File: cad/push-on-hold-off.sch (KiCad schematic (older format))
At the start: 12 parts

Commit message: Annotate schematic
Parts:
- gave numbers to parts that had none: 11
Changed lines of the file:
@@
 LIBS:contrib
 LIBS:valves
+LIBS:push-on-hold-off-cache
 EELAYER 25 0
 EELAYER END
@@
 $EndDescr
 $Comp
-L IRF7309IPBF Q?
+L IRF7309IPBF Q1
 U 1 1 569FBD83
 P 6050 4300
-F 0 "Q?" H 6300 4375 50  0000 L CNN
+F 0 "Q1" H 6300 4375 50  0000 L CNN
 F 1 "IRF7309IPBF" H 6300 4300 50  0000 L CNN
 F 2 "SO-8" H 6300 4225 50  0000 L CNN
@@
 $EndComp
 $Comp
-L IRF7309IPBF Q?
+L IRF7309IPBF Q1
 U 2 1 569FBDAC
 P 6000 3700
-F 0 "Q?" H 6250 3775 50  0000 L CNN
+F 0 "Q1" H 6250 3775 50  0000 L CNN
 F 1 "IRF7309IPBF" H 6250 3700 50  0000 L CNN
 F 2 "SO-8" H 6250 3625 50  0000 L CNN
@@
 $EndComp
 $Comp
-L CONN_01X04 P?
+L CONN_01X04 P1
 U 1 1 569FC392
 P 4450 3750
-F 0 "P?" H 4450 4000 50  0000 C CNN
+F 0 "P1" H 4450 4000 50  0000 C CNN
 F 1 "CONN_01X04" V 4550 3750 50  0000 C CNN
 F 2 "" H 4450 3750 60  0000 C CNN
@@
 $EndComp
 $Comp
-L R R?
+L R R1
 U 1 1 569FC430
 P 5050 3800
-F 0 "R?" V 5130 3800 50  0000 C CNN
+F 0 "R1" V 5130 3800 50  0000 C CNN
 F 1 "10k" V 5050 3800 50  0000 C CNN
 F 2 "" V 4980 3800 30  0000 C CNN
@@
 $EndComp
 $Comp
-L R R?
+L R R2
 U 1 1 569FC492
 P 5650 3800
-F 0 "R?" V 5730 3800 50  0000 C CNN
+F 0 "R2" V 5730 3800 50  0000 C CNN
 F 1 "100k" V 5650 3800 50  0000 C CNN
 F 2 "" V 5580 3800 30  0000 C CNN
@@
 	4650 3600 5800 3600
 $Comp
-L C C?
+L C C1
 U 1 1 569FC537
 P 5350 4100
-F 0 "C?" H 5375 4200 50  0000 L CNN
+F 0 "C1" H 5375 4200 50  0000 L CNN
 F 1 "1uF" H 5375 4000 50  0000 L CNN
 F 2 "" H 5388 3950 30  0000 C CNN
@@
 	5950 4100 5950 3900
 $Comp
-L GND #PWR?
+L GND #PWR1
 U 1 1 569FC7CE
 P 4700 4050
-F 0 "#PWR?" H 4700 3800 50  0001 C CNN
+F 0 "#PWR1" H 4700 3800 50  0001 C CNN
 F 1 "GND" H 4700 3900 50  0000 C CNN
 F 2 "" H 4700 4050 60  0000 C CNN
@@
 Wire Wire Line
 	4850 4100 5200 4100
-Text Label 4750 3700 0    60   ~ 0
+Text Label 4650 3700 0    60   ~ 0
 Button
 $Comp
-L D D?
+L D D1
 U 1 1 569FCB4E
 P 4850 4400
-F 0 "D?" H 4850 4500 50  0000 C CNN
+F 0 "D1" H 4850 4500 50  0000 C CNN
 F 1 "D" H 4850 4300 50  0000 C CNN
 F 2 "" H 4850 4400 60  0000 C CNN
@@
 Connection ~ 5850 4100
 $Comp
-L GND #PWR?
+L GND #PWR2
 U 1 1 569FCD58
 P 5950 4550
-F 0 "#PWR?" H 5950 4300 50  0001 C CNN
+F 0 "#PWR2" H 5950 4300 50  0001 C CNN
 F 1 "GND" H 5950 4400 50  0000 C CNN
 F 2 "" H 5950 4550 60  0000 C CNN
@@
 	5950 4500 5950 4550
 $Comp
-L C C?
+L C C2
 U 1 1 569FCE3F
 P 6500 3950
-F 0 "C?" H 6525 4050 50  0000 L CNN
+F 0 "C2" H 6525 4050 50  0000 L CNN
 F 1 "10uF" H 6525 3850 50  0000 L CNN
 F 2 "" H 6538 3800 30  0000 C CNN
@@
 Connection ~ 6300 3600
 $Comp
-L CONN_01X04 P?
+L CONN_01X04 P2
 U 1 1 569FCF63
 P 7750 3750
-F 0 "P?" H 7750 4000 50  0000 C CNN
+F 0 "P2" H 7750 4000 50  0000 C CNN
 F 1 "CONN_01X04" V 7850 3750 50  0000 C CNN
 F 2 "" H 7750 3750 60  0000 C CNN
@@
 $EndComp
 $Comp
-L R R?
+L R R4
 U 1 1 569FD783
 P 6950 3950
-F 0 "R?" V 7030 3950 50  0000 C CNN
+F 0 "R4" V 7030 3950 50  0000 C CNN
 F 1 "100k" V 6950 3950 50  0000 C CNN
 F 2 "" V 6880 3950 30  0000 C CNN
@@
 Connection ~ 6500 4350
 $Comp
-L R R?
+L R R3
 U 1 1 569FD864
 P 6700 4350
-F 0 "R?" V 6780 4350 50  0000 C CNN
+F 0 "R3" V 6780 4350 50  0000 C CNN
 F 1 "300k" V 6700 4350 50  0000 C CNN
 F 2 "" V 6630 4350 30  0000 C CNN
@@
 Text Label 7300 3600 0    60   ~ 0
 Vout
-Text Label 4750 3600 0    60   ~ 0
+Text Label 4650 3600 0    60   ~ 0
 Vin
 Text Label 7300 3700 0    60   ~ 0
@@
 	7550 3700 7300 3700
 $Comp
-L GND #PWR?
+L GND #PWR4
 U 1 1 569FDE5F
 P 7450 3950
-F 0 "#PWR?" H 7450 3700 50  0001 C CNN
+F 0 "#PWR4" H 7450 3700 50  0001 C CNN
 F 1 "GND" H 7450 3800 50  0000 C CNN
 F 2 "" H 7450 3950 60  0000 C CNN
@@
 Connection ~ 6950 4350
 $Comp
-L SW_PUSH_SMALL SW?
+L SW_PUSH_SMALL SW1
 U 1 1 569FEA9F
 P 5950 5350
-F 0 "SW?" H 6100 5460 30  0000 C CNN
+F 0 "SW1" H 6100 5460 30  0000 C CNN
 F 1 "SW_PUSH_SMALL" H 5950 5271 30  0000 C CNN
 F 2 "" H 5950 5350 60  0000 C CNN
@@
 $EndComp
 $Comp
-L GND #PWR?
+L GND #PWR3
 U 1 1 569FECE2
 P 6100 5500
-F 0 "#PWR?" H 6100 5250 50  0001 C CNN
+F 0 "#PWR3" H 6100 5250 50  0001 C CNN
 F 1 "GND" H 6100 5350 50  0000 C CNN
 F 2 "" H 6100 5500 60  0000 C CNN

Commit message: Start layout
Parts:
- C1, C2: footprint (none) -> Capacitors_SMD.pretty:C_0603_HandSoldering
- D1: footprint (none) -> Diodes_SMD.pretty:SOD-323; Farnell (none) -> 1466524
- P1, P2: footprint (none) -> Pin_Headers.pretty:Pin_Header_Straight_1x04
- Q1: footprint SO-8 -> Housings_SOIC.pretty:SOIJ-8_5.3x5.3mm_Pitch1.27mm; Farnell (none) -> 2468006
- Q1: footprint SO-8 -> Housings_SOIC.pretty:SOIJ-8_5.3x5.3mm_Pitch1.27mm
- R1, R2, R3, R4: footprint (none) -> Resistors_SMD.pretty:R_0603_HandSoldering
- SW1: footprint (none) -> Buttons_Switches_SMD.pretty:SW_SPST_EVPBF; Farnell (none) -> 3801305
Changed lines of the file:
@@
 F 0 "Q1" H 6300 4375 50  0000 L CNN
 F 1 "IRF7309IPBF" H 6300 4300 50  0000 L CNN
-F 2 "SO-8" H 6300 4225 50  0000 L CNN
+F 2 "Housings_SOIC.pretty:SOIJ-8_5.3x5.3mm_Pitch1.27mm" H 6300 4225 50  0000 L CNN
 F 3 "" H 6050 4300 50  0000 L CNN
+F 4 "2468006" H 6050 4300 60  0001 C CNN "Farnell"
 	1    6050 4300
 	-1   0    0    -1
@@
 F 0 "Q1" H 6250 3775 50  0000 L CNN
 F 1 "IRF7309IPBF" H 6250 3700 50  0000 L CNN
-F 2 "SO-8" H 6250 3625 50  0000 L CNN
+F 2 "Housings_SOIC.pretty:SOIJ-8_5.3x5.3mm_Pitch1.27mm" H 6250 3625 50  0000 L CNN
 F 3 "" H 6000 3700 50  0000 L CNN
 	2    6000 3700
@@
 F 0 "P1" H 4450 4000 50  0000 C CNN
 F 1 "CONN_01X04" V 4550 3750 50  0000 C CNN
-F 2 "" H 4450 3750 60  0000 C CNN
+F 2 "Pin_Headers.pretty:Pin_Header_Straight_1x04" H 4450 3750 60  0001 C CNN
 F 3 "" H 4450 3750 60  0000 C CNN
 	1    4450 3750
@@
 F 0 "R1" V 5130 3800 50  0000 C CNN
 F 1 "10k" V 5050 3800 50  0000 C CNN
-F 2 "" V 4980 3800 30  0000 C CNN
+F 2 "Resistors_SMD.pretty:R_0603_HandSoldering" V 4980 3800 30  0001 C CNN
 F 3 "" H 5050 3800 30  0000 C CNN
 	1    5050 3800
@@
 F 0 "R2" V 5730 3800 50  0000 C CNN
 F 1 "100k" V 5650 3800 50  0000 C CNN
-F 2 "" V 5580 3800 30  0000 C CNN
+F 2 "Resistors_SMD.pretty:R_0603_HandSoldering" V 5580 3800 30  0001 C CNN
 F 3 "" H 5650 3800 30  0000 C CNN
 	1    5650 3800
@@
 F 0 "C1" H 5375 4200 50  0000 L CNN
 F 1 "1uF" H 5375 4000 50  0000 L CNN
-F 2 "" H 5388 3950 30  0000 C CNN
+F 2 "Capacitors_SMD.pretty:C_0603_HandSoldering" H 5388 3950 30  0001 C CNN
 F 3 "" H 5350 4100 60  0000 C CNN
 	1    5350 4100
@@
 	5950 4100 5950 3900
 $Comp
-L GND #PWR1
+L GND #PWR01
 U 1 1 569FC7CE
 P 4700 4050
-F 0 "#PWR1" H 4700 3800 50  0001 C CNN
+F 0 "#PWR01" H 4700 3800 50  0001 C CNN
 F 1 "GND" H 4700 3900 50  0000 C CNN
 F 2 "" H 4700 4050 60  0000 C CNN
@@
 F 0 "D1" H 4850 4500 50  0000 C CNN
 F 1 "D" H 4850 4300 50  0000 C CNN
-F 2 "" H 4850 4400 60  0000 C CNN
+F 2 "Diodes_SMD.pretty:SOD-323" H 4850 4400 60  0001 C CNN
 F 3 "" H 4850 4400 60  0000 C CNN
+F 4 "1466524" H 4850 4400 60  0001 C CNN "Farnell"
 	1    4850 4400
 	0    1    1    0
@@
 Connection ~ 5850 4100
 $Comp
-L GND #PWR2
+L GND #PWR02
 U 1 1 569FCD58
 P 5950 4550
-F 0 "#PWR2" H 5950 4300 50  0001 C CNN
+F 0 "#PWR02" H 5950 4300 50  0001 C CNN
 F 1 "GND" H 5950 4400 50  0000 C CNN
 F 2 "" H 5950 4550 60  0000 C CNN
@@
 F 0 "C2" H 6525 4050 50  0000 L CNN
 F 1 "10uF" H 6525 3850 50  0000 L CNN
-F 2 "" H 6538 3800 30  0000 C CNN
+F 2 "Capacitors_SMD.pretty:C_0603_HandSoldering" H 6538 3800 30  0001 C CNN
 F 3 "" H 6500 3950 60  0000 C CNN
 	1    6500 3950
@@
 F 0 "P2" H 7750 4000 50  0000 C CNN
 F 1 "CONN_01X04" V 7850 3750 50  0000 C CNN
-F 2 "" H 7750 3750 60  0000 C CNN
+F 2 "Pin_Headers.pretty:Pin_Header_Straight_1x04" H 7750 3750 60  0001 C CNN
 F 3 "" H 7750 3750 60  0000 C CNN
 	1    7750 3750
@@
 F 0 "R4" V 7030 3950 50  0000 C CNN
 F 1 "100k" V 6950 3950 50  0000 C CNN
-F 2 "" V 6880 3950 30  0000 C CNN
+F 2 "Resistors_SMD.pretty:R_0603_HandSoldering" V 6880 3950 30  0001 C CNN
 F 3 "" H 6950 3950 30  0000 C CNN
 	1    6950 3950
@@
 F 0 "R3" V 6780 4350 50  0000 C CNN
 F 1 "300k" V 6700 4350 50  0000 C CNN
-F 2 "" V 6630 4350 30  0000 C CNN
+F 2 "Resistors_SMD.pretty:R_0603_HandSoldering" V 6630 4350 30  0001 C CNN
 F 3 "" H 6700 4350 30  0000 C CNN
 	1    6700 4350
@@
 	7550 3700 7300 3700
 $Comp
-L GND #PWR4
+L GND #PWR03
 U 1 1 569FDE5F
 P 7450 3950
-F 0 "#PWR4" H 7450 3700 50  0001 C CNN
+F 0 "#PWR03" H 7450 3700 50  0001 C CNN
 F 1 "GND" H 7450 3800 50  0000 C CNN
 F 2 "" H 7450 3950 60  0000 C CNN
@@
 F 0 "SW1" H 6100 5460 30  0000 C CNN
 F 1 "SW_PUSH_SMALL" H 5950 5271 30  0000 C CNN
-F 2 "" H 5950 5350 60  0000 C CNN
+F 2 "Buttons_Switches_SMD.pretty:SW_SPST_EVPBF" H 5950 5350 60  0001 C CNN
 F 3 "" H 5950 5350 60  0000 C CNN
+F 4 "3801305" H 5950 5350 60  0001 C CNN "Farnell"
 	1    5950 5350
 	1    0    0    -1
 $EndComp
 $Comp
-L GND #PWR3
+L GND #PWR04
 U 1 1 569FECE2
 P 6100 5500
-F 0 "#PWR3" H 6100 5250 50  0001 C CNN
+F 0 "#PWR04" H 6100 5250 50  0001 C CNN
 F 1 "GND" H 6100 5350 50  0000 C CNN
 F 2 "" H 6100 5500 60  0000 C CNN

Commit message: Add silkscreen connection reference
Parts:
- D1: Farnell 1466524 -> (none); Vendor (none) -> 1466524
- Q1: Farnell 2468006 -> (none); Vendor (none) -> 2468006
- SW1: Farnell 3801305 -> (none); Vendor (none) -> 3801305
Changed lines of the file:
@@
 F 2 "Housings_SOIC.pretty:SOIJ-8_5.3x5.3mm_Pitch1.27mm" H 6300 4225 50  0000 L CNN
 F 3 "" H 6050 4300 50  0000 L CNN
-F 4 "2468006" H 6050 4300 60  0001 C CNN "Farnell"
+F 4 "2468006" H 6050 4300 60  0001 C CNN "Vendor"
 	1    6050 4300
 	-1   0    0    -1
@@
 F 2 "Diodes_SMD.pretty:SOD-323" H 4850 4400 60  0001 C CNN
 F 3 "" H 4850 4400 60  0000 C CNN
-F 4 "1466524" H 4850 4400 60  0001 C CNN "Farnell"
+F 4 "1466524" H 4850 4400 60  0001 C CNN "Vendor"
 	1    4850 4400
 	0    1    1    0
@@
 F 2 "Buttons_Switches_SMD.pretty:SW_SPST_EVPBF" H 5950 5350 60  0001 C CNN
 F 3 "" H 5950 5350 60  0000 C CNN
-F 4 "3801305" H 5950 5350 60  0001 C CNN "Farnell"
+F 4 "3801305" H 5950 5350 60  0001 C CNN "Vendor"
 	1    5950 5350
 	1    0    0    -1

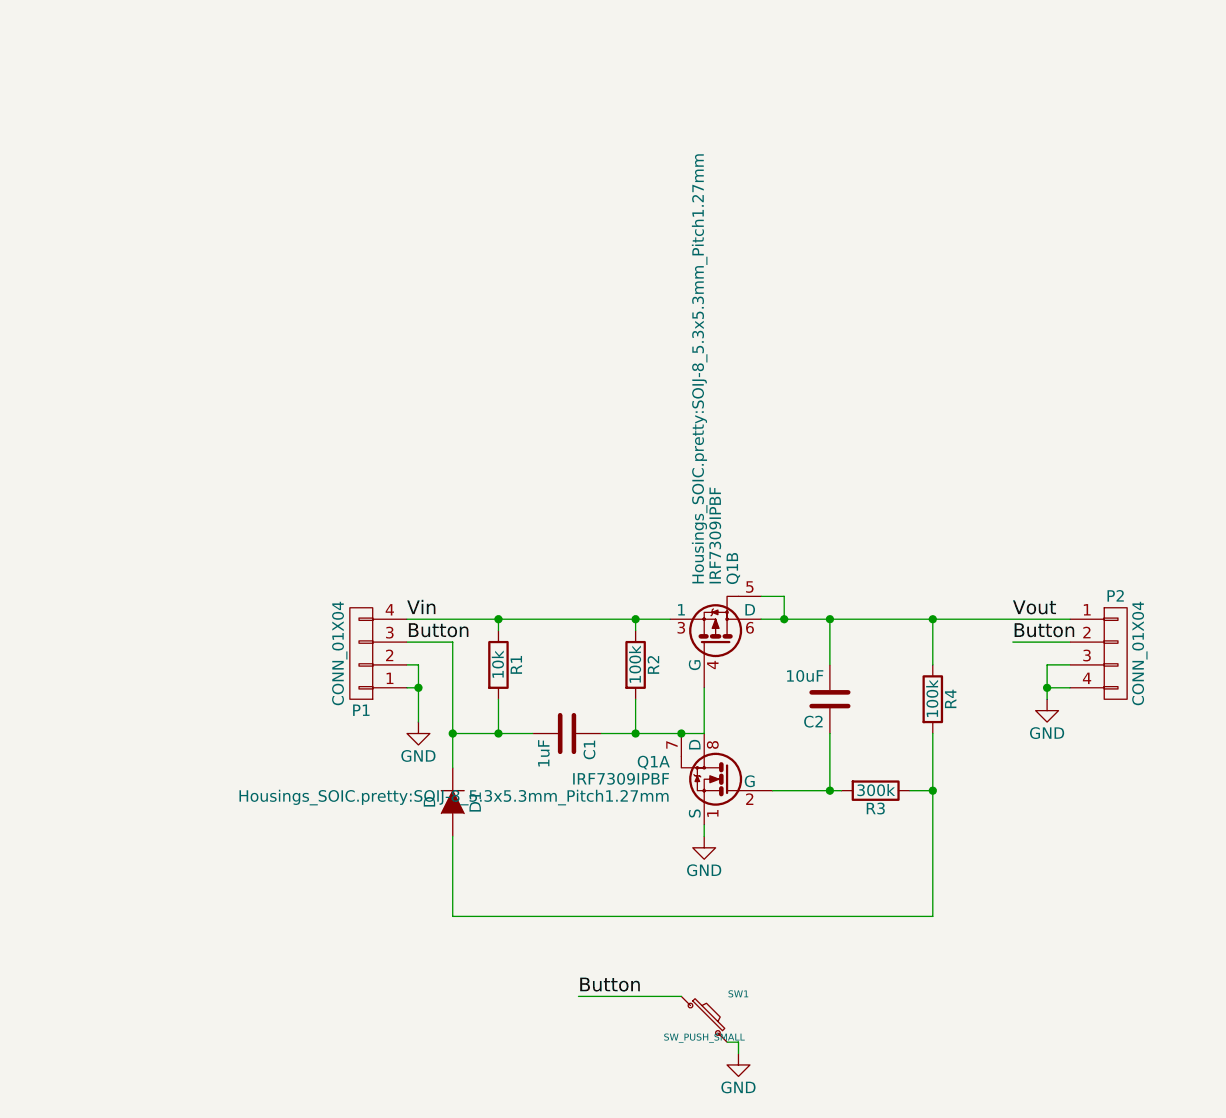
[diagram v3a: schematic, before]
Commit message: Add auto/on off caps and change Q1 footprint
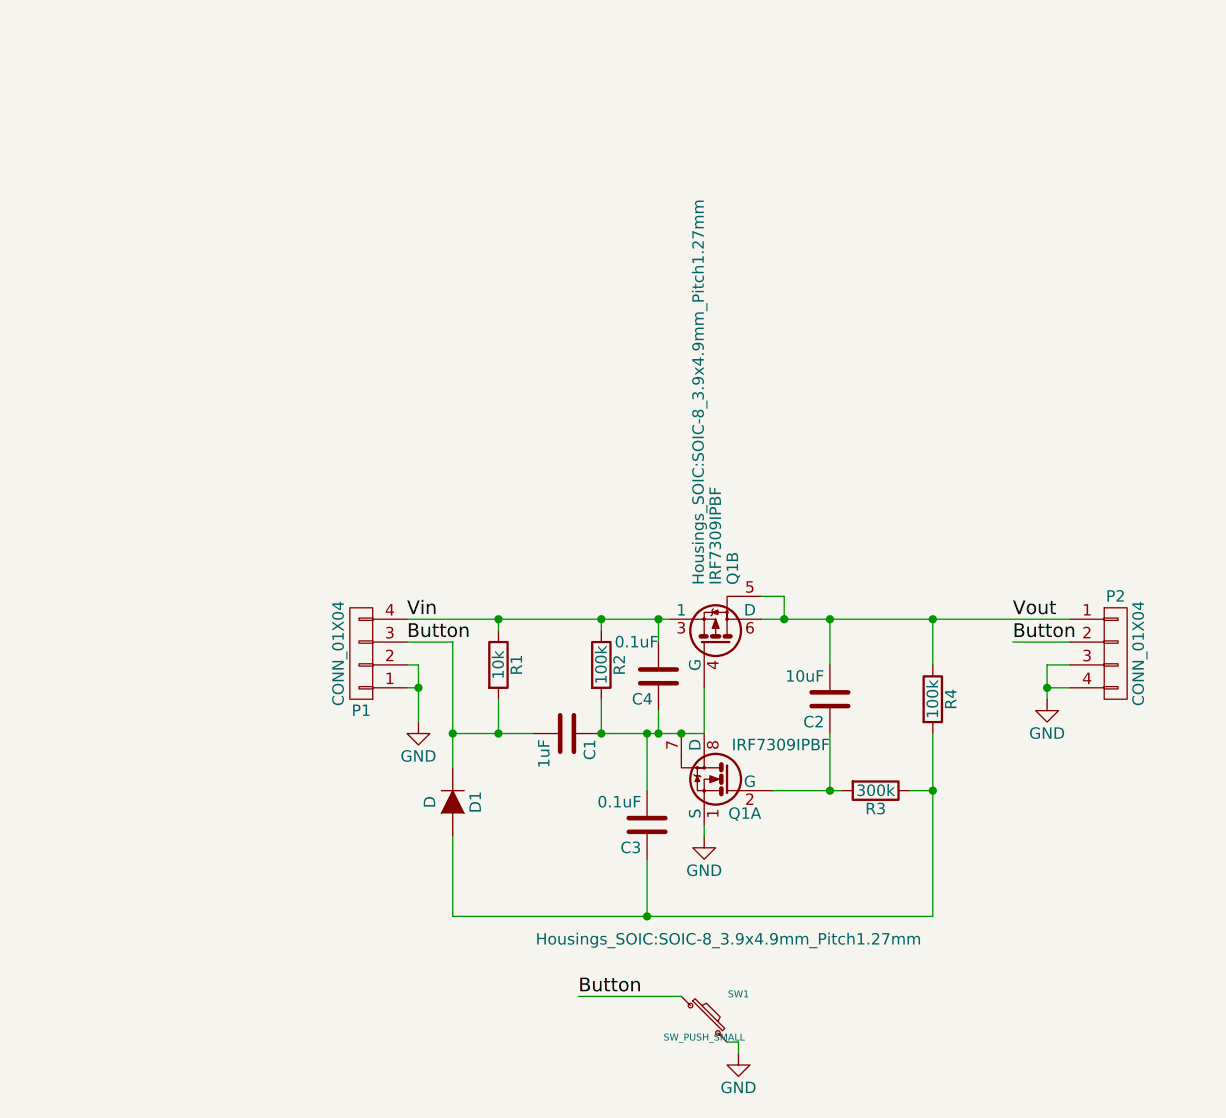
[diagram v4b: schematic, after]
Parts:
- added C3, C4: 0.1uF, Capacitors_SMD.pretty:C_0603_HandSoldering, symbol C
- Q1: footprint Housings_SOIC.pretty:SOIJ-8_5.3x5.3mm_Pitch1.27mm -> Housings_SOIC:SOIC-8_3.9x4.9mm_Pitch1.27mm
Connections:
- net Vin: now also C4.2
- net at C1.1, Q1.4 (G), Q1.7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: now also C3.2, C4.1
- net at D1.2 (A), R3.1, R4.2: now also C3.1
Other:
- moved on the sheet: R2
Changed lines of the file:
@@
 U 1 1 569FBD83
 P 6050 4300
-F 0 "Q1" H 6300 4375 50  0000 L CNN
-F 1 "IRF7309IPBF" H 6300 4300 50  0000 L CNN
-F 2 "Housings_SOIC.pretty:SOIJ-8_5.3x5.3mm_Pitch1.27mm" H 6300 4225 50  0000 L CNN
+F 0 "Q1" H 5900 4150 50  0000 L CNN
+F 1 "IRF7309IPBF" H 5600 4450 50  0000 L CNN
+F 2 "Housings_SOIC:SOIC-8_3.9x4.9mm_Pitch1.27mm" H 5200 3600 50  0000 L CNN
 F 3 "" H 6050 4300 50  0000 L CNN
 F 4 "2468006" H 6050 4300 60  0001 C CNN "Vendor"
@@
 F 0 "Q1" H 6250 3775 50  0000 L CNN
 F 1 "IRF7309IPBF" H 6250 3700 50  0000 L CNN
-F 2 "Housings_SOIC.pretty:SOIJ-8_5.3x5.3mm_Pitch1.27mm" H 6250 3625 50  0000 L CNN
+F 2 "Housings_SOIC:SOIC-8_3.9x4.9mm_Pitch1.27mm" H 6250 3625 50  0000 L CNN
 F 3 "" H 6000 3700 50  0000 L CNN
 	2    6000 3700
@@
 L R R2
 U 1 1 569FC492
-P 5650 3800
-F 0 "R2" V 5730 3800 50  0000 C CNN
-F 1 "100k" V 5650 3800 50  0000 C CNN
-F 2 "Resistors_SMD.pretty:R_0603_HandSoldering" V 5580 3800 30  0001 C CNN
-F 3 "" H 5650 3800 30  0000 C CNN
-	1    5650 3800
-	1    0    0    -1
-$EndComp
-Wire Wire Line
-	4650 3600 5800 3600
+P 5500 3800
+F 0 "R2" V 5580 3800 50  0000 C CNN
+F 1 "100k" V 5500 3800 50  0000 C CNN
+F 2 "Resistors_SMD.pretty:R_0603_HandSoldering" V 5430 3800 30  0001 C CNN
+F 3 "" H 5500 3800 30  0000 C CNN
+	1    5500 3800
+	1    0    0    -1
+$EndComp
 $Comp
 L C C1
@@
 	0    1    1    0
 $EndComp
-Wire Wire Line
-	5050 3650 5050 3600
-Connection ~ 5050 3600
-Connection ~ 5650 3600
-Wire Wire Line
-	5500 4100 5950 4100
-Wire Wire Line
-	5950 4100 5950 3900
 $Comp
 L GND #PWR01
@@
 	1    0    0    -1
 $EndComp
-Wire Wire Line
-	4650 3800 4700 3800
-Wire Wire Line
-	4700 3800 4700 4050
-Wire Wire Line
-	4650 3900 4700 3900
-Connection ~ 4700 3900
-Wire Wire Line
-	4650 3700 4850 3700
-Wire Wire Line
-	4850 3700 4850 4250
-Wire Wire Line
-	5650 3600 5650 3650
-Wire Wire Line
-	5650 3950 5650 4100
-Connection ~ 5650 4100
-Wire Wire Line
-	5050 3950 5050 4100
-Connection ~ 5050 4100
-Wire Wire Line
-	4850 4100 5200 4100
 Text Label 4650 3700 0    60   ~ 0
 Button
@@
 	0    1    1    0
 $EndComp
-Connection ~ 4850 4100
-Connection ~ 5850 4100
 $Comp
 L GND #PWR02
@@
 	1    0    0    -1
 $EndComp
-Wire Wire Line
-	5950 4500 5950 4550
 $Comp
 L C C2
@@
 	-1   0    0    1
 $EndComp
-Wire Wire Line
-	6500 4350 6500 4100
-Wire Wire Line
-	6500 3600 6500 3800
-Wire Wire Line
-	6200 3600 7550 3600
-Wire Wire Line
-	6300 3600 6300 3500
-Wire Wire Line
-	6300 3500 6200 3500
-Connection ~ 6300 3600
 $Comp
 L CONN_01X04 P2
@@
 	1    0    0    -1
 $EndComp
-Wire Wire Line
-	6950 3600 6950 3800
-Connection ~ 6500 3600
-Wire Wire Line
-	6950 4100 6950 4900
-Connection ~ 6500 4350
 $Comp
 L R R3
@@
 	0    1    1    0
 $EndComp
-Wire Wire Line
-	6250 4350 6550 4350
-Wire Wire Line
-	6950 4350 6850 4350
-Connection ~ 6950 3600
 Text Label 7300 3600 0    60   ~ 0
 Vout
@@
 Text Label 7300 3700 0    60   ~ 0
 Button
-Wire Wire Line
-	7550 3700 7300 3700
 $Comp
 L GND #PWR03
@@
 	1    0    0    -1
 $EndComp
-Wire Wire Line
-	7550 3900 7450 3900
-Wire Wire Line
-	7450 3800 7450 3950
-Wire Wire Line
-	7550 3800 7450 3800
-Connection ~ 7450 3900
-Wire Wire Line
-	4850 4550 4850 4900
-Wire Wire Line
-	4850 4900 6950 4900
-Connection ~ 6950 4350
 $Comp
 L SW_PUSH_SMALL SW1
@@
 	1    0    0    -1
 $EndComp
-Wire Wire Line
-	6050 5450 6100 5450
-Wire Wire Line
-	6100 5450 6100 5500
 Text Label 5400 5250 0    60   ~ 0
 Button
+$Comp
+L C C4
+U 1 1 57563AC8
+P 5750 3850
+F 0 "C4" H 5775 3950 50  0000 L CNN
+F 1 "0.1uF" H 5750 3700 50  0000 L CNN
+F 2 "Capacitors_SMD.pretty:C_0603_HandSoldering" H 5788 3700 30  0001 C CNN
+F 3 "" H 5750 3850 60  0000 C CNN
+	1    5750 3850
+	-1   0    0    1
+$EndComp
+$Comp
+L C C3
+U 1 1 57563BCA
+P 5700 4500
+F 0 "C3" H 5725 4600 50  0000 L CNN
+F 1 "0.1uF" H 5725 4400 50  0000 L CNN
+F 2 "Capacitors_SMD.pretty:C_0603_HandSoldering" H 5738 4350 30  0001 C CNN
+F 3 "" H 5700 4500 60  0000 C CNN
+	1    5700 4500
+	-1   0    0    1
+$EndComp
+Wire Wire Line
+	4650 3600 5800 3600
+Wire Wire Line
+	5050 3650 5050 3600
+Connection ~ 5050 3600
+Connection ~ 5500 3600
+Wire Wire Line
+	5500 4100 5950 4100
+Wire Wire Line
+	5950 4100 5950 3900
+Wire Wire Line
+	4650 3800 4700 3800
+Wire Wire Line
+	4700 3800 4700 4050
+Wire Wire Line
+	4650 3900 4700 3900
+Connection ~ 4700 3900
+Wire Wire Line
+	4650 3700 4850 3700
+Wire Wire Line
+	4850 3700 4850 4250
+Wire Wire Line
+	5500 3600 5500 3650
+Wire Wire Line
+	5500 3950 5500 4100
+Connection ~ 5500 4100
+Wire Wire Line
+	5050 3950 5050 4100
+Connection ~ 5050 4100
+Wire Wire Line
+	4850 4100 5200 4100
+Connection ~ 4850 4100
+Connection ~ 5850 4100
+Wire Wire Line
+	5950 4500 5950 4550
+Wire Wire Line
+	6500 4350 6500 4100
+Wire Wire Line
+	6500 3600 6500 3800
+Wire Wire Line
+	6200 3600 7550 3600
+Wire Wire Line
+	6300 3600 6300 3500
+Wire Wire Line
+	6300 3500 6200 3500
+Connection ~ 6300 3600
+Wire Wire Line
+	6950 3600 6950 3800
+Connection ~ 6500 3600
+Wire Wire Line
+	6950 4900 6950 4100
+Connection ~ 6500 4350
+Wire Wire Line
+	6250 4350 6550 4350
+Wire Wire Line
+	6950 4350 6850 4350
+Connection ~ 6950 3600
+Wire Wire Line
+	7550 3700 7300 3700
+Wire Wire Line
+	7550 3900 7450 3900
+Wire Wire Line
+	7450 3800 7450 3950
+Wire Wire Line
+	7550 3800 7450 3800
+Connection ~ 7450 3900
+Wire Wire Line
+	4850 4550 4850 4900
+Wire Wire Line
+	4850 4900 6950 4900
+Connection ~ 6950 4350
+Wire Wire Line
+	6050 5450 6100 5450
+Wire Wire Line
+	6100 5450 6100 5500
 Wire Wire Line
 	5850 5250 5400 5250
+Wire Wire Line
+	5700 4100 5700 4350
+Connection ~ 5700 4100
+Wire Wire Line
+	5750 3700 5750 3600
+Connection ~ 5750 3600
+Wire Wire Line
+	5700 4650 5700 4900
+Connection ~ 5700 4900
+Wire Wire Line
+	5750 4100 5750 4000
+Connection ~ 5750 4100
 $EndSCHEMATC

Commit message: Switch diode to bigger package
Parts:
- D1: footprint Diodes_SMD.pretty:SOD-323 -> Diodes_SMD:SMA_Standard
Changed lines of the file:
@@
 F 0 "D1" H 4850 4500 50  0000 C CNN
 F 1 "D" H 4850 4300 50  0000 C CNN
-F 2 "Diodes_SMD.pretty:SOD-323" H 4850 4400 60  0001 C CNN
+F 2 "Diodes_SMD:SMA_Standard" H 4850 4400 60  0001 C CNN
 F 3 "" H 4850 4400 60  0000 C CNN
 F 4 "1466524" H 4850 4400 60  0001 C CNN "Vendor"
